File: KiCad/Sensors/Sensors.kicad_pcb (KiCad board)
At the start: 2 copper layers, 36.8 x 19 mm, 13 parts, among them J1 Conn_2Rows-11Pins, J2 Conn_01x04, U1 OPA1641

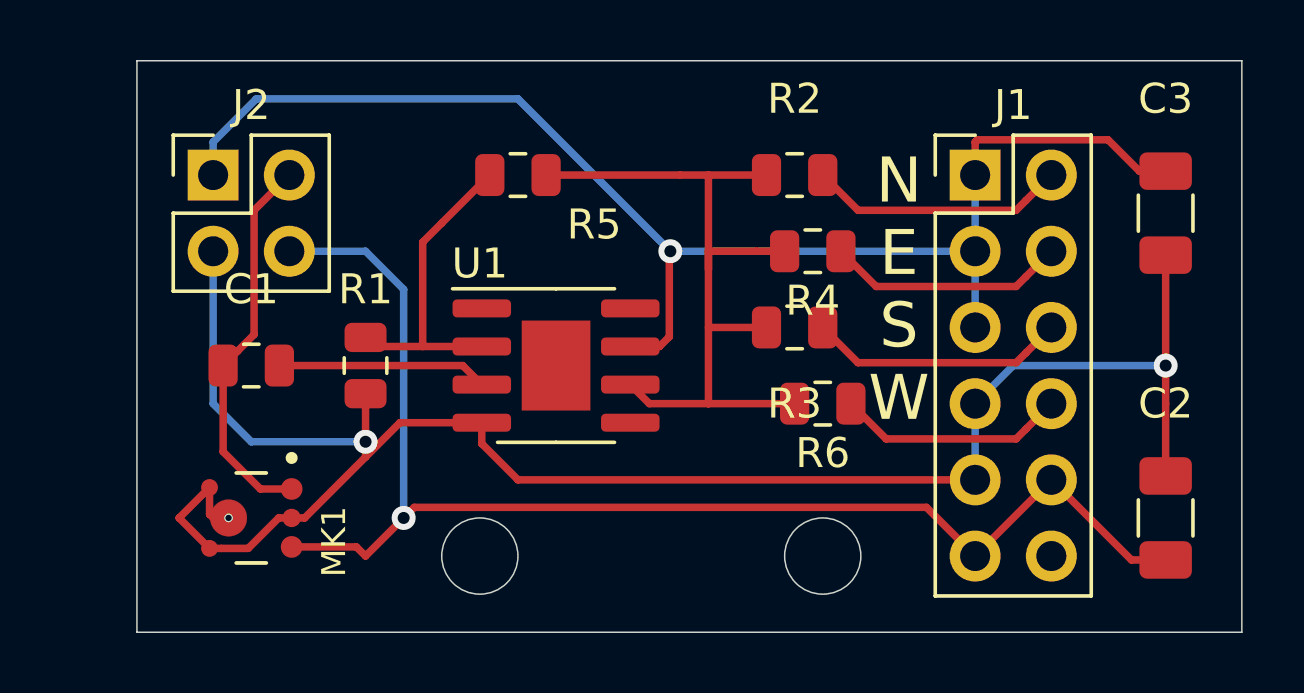
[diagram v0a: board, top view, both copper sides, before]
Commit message: Sensor Module
This commit updates the sensor module  for experimental evaluation
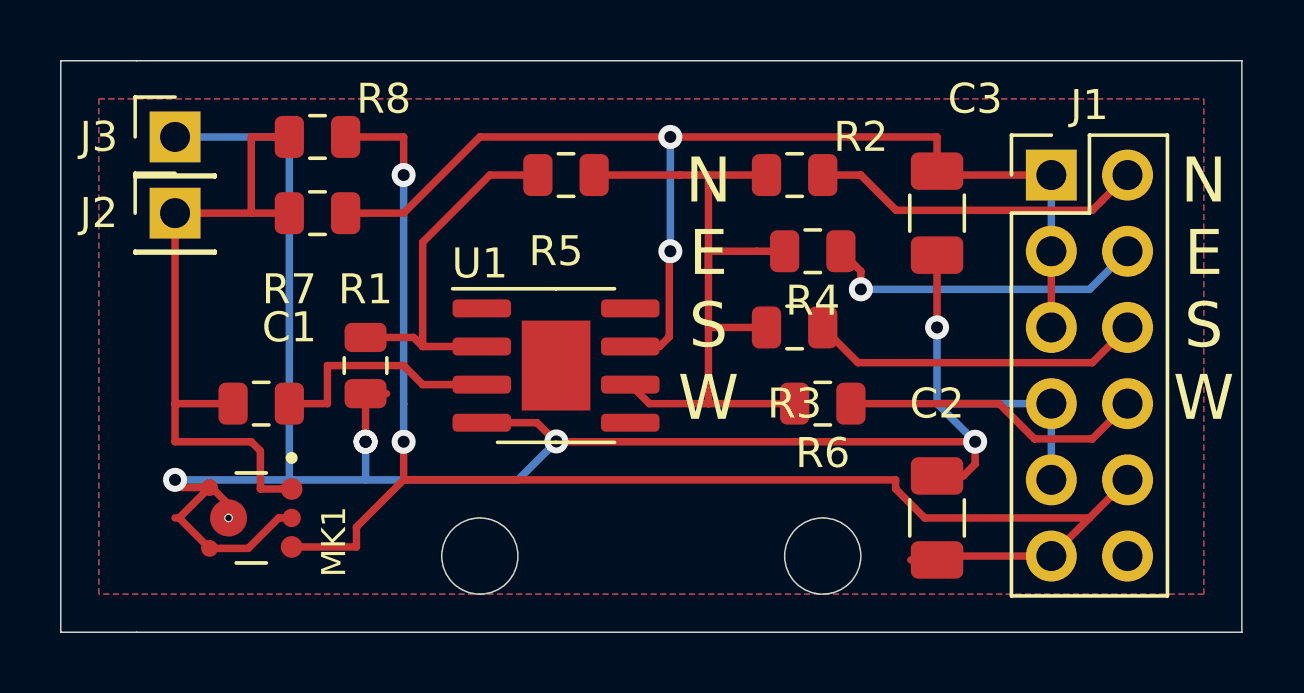
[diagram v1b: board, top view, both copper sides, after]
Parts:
- added J3: Conn_01x01, Connector_PinHeader_2.54mm:PinHeader_1x01_P2.54mm_Vertical, F.Cu at (127.0, 80.0)
- added R7: 10k0, Resistor_SMD:R_0805_2012Metric, F.Cu at (131.7, 82.5)
- added R8: 10K0, Resistor_SMD:R_0805_2012Metric, F.Cu at (131.7, 80.0)
- J2: value Conn_01x04 -> Conn_01x01; footprint Connector_PinHeader_2.54mm:PinHeader_2x02_P2.54mm_Vertical -> Connector_PinHeader_2.54mm:PinHeader_1x01_P2.54mm_Vertical
- moved C2 7.62 mm to (152.4, 92.7)
- moved C3 7.62 mm to (152.4, 82.5)
- moved J1 2.54 mm to (156.2, 81.3)
- moved J2 1.80 mm to (127.0, 82.5)
- moved R5 1.60 mm to (140.0, 81.3)
- moved C1 1.31 mm to (129.9, 88.9)
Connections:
- C2 pad 1: Net-(C2-Pad1) -> +3V3
- C2 pad 2: Net-(C2-Pad2) -> GND
- C3 pad 1: Net-(C3-Pad1) -> VCC
- C3 pad 2: Net-(C2-Pad2) -> GND
- J1 pad 1: Net-(C3-Pad1) -> VCC
- J1 pad 10: Net-(C2-Pad1) -> +3V3
- J1 pad 11: Net-(C2-Pad1) -> +3V3
- J1 pad 3: Net-(C3-Pad1) -> VCC
- J1 pad 5: Net-(C3-Pad1) -> VCC
- J1 pad 7: Net-(C2-Pad2) -> GND
- J1 pad 9: Net-(C2-Pad2) -> GND
- J2 pad 1: Net-(C3-Pad1) -> Net-(C1-Pad2)
- MK1 pad 2: Net-(C2-Pad2) -> GND
- MK1 pad 3: Net-(C2-Pad2) -> GND
- MK1 pad 4: Net-(C2-Pad1) -> +3V3
- MK1 pad 5: Net-(C2-Pad2) -> GND
- MK1 pad 6: Net-(C2-Pad2) -> GND
- R1 pad 2: Net-(C2-Pad2) -> GND
- U1 pad 4: Net-(C2-Pad2) -> GND
- U1 pad 7: Net-(C3-Pad1) -> VCC
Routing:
- net GND: track 0.00 -> 72.5 mm, vias 0 -> 6
- net Net-(C2-Pad2): track 62.0 -> 0.00 mm, vias 2 -> 0
- net +3V3: track 0.00 -> 50.5 mm, vias 0 -> 2
- net Net-(C3-Pad1): track 46.5 -> 0.00 mm, vias 1 -> 0
- net Net-(C2-Pad1): track 44.9 -> 0.00 mm, vias 1 -> 0
- net VCC: track 0.00 -> 39.1 mm, vias 0 -> 2
- net Net-(C1-Pad2): track 12.9 -> 22.5 mm
- net Net-(J1-Pad4): track 7.99 -> 11.0 mm, vias 0 -> 1
- net Net-(J1-Pad8): track 7.66 -> 10.2 mm
- net Net-(J1-Pad6): track 8.59 -> 11.1 mm
- net Net-(J1-Pad2): track 8.78 -> 11.1 mm
- net Net-(R1-Pad1): track 10.6 -> 12.7 mm
- net Net-(R2-Pad1): track 25.8 -> 24.2 mm
- net Net-(C1-Pad1): track 7.01 -> 7.95 mm
- added copper zone on B.Cu, net GND
- added copper zone on F.Cu, net VCC
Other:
- board size 36.8 x 19 mm -> 39.4 x 19 mm
